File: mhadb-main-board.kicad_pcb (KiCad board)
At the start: 4 copper layers, 50 x 50 mm, 109 parts, among them J1 Conn_01x04, J10 Conn_01x04_Pin, J2 Conn_01x04, J3 USB_C_Receptacle_USB2.0_14P, J4 Conn_01x02, J5 Conn_01x03, J6 Conn_01x03, J7 Conn_01x04, J8 Conn_01x04, J9 Conn_01x02_Pin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

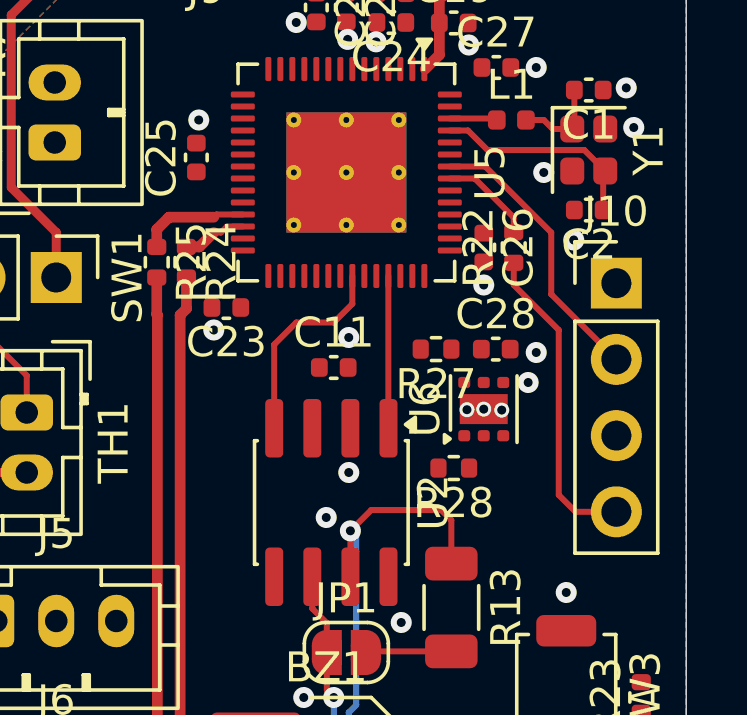
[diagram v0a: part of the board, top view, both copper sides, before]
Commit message: pcb: add I2C routing
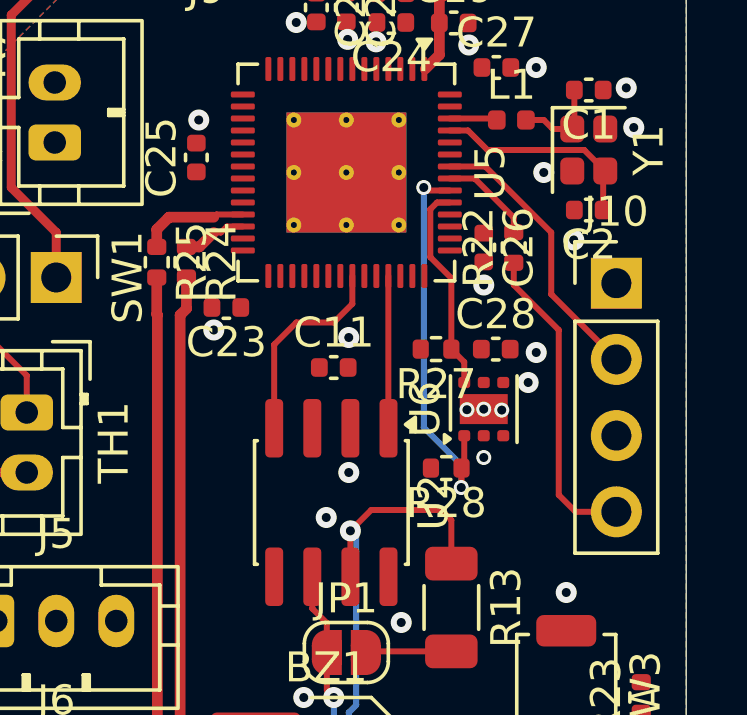
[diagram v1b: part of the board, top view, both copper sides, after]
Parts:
- moved R28 0.25 mm to (146.0, 73.4)
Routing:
- net /SCL: track 0.00 -> 13.2 mm, vias 0 -> 2
- net /SDA: track 0.00 -> 6.99 mm
- net GND: vias 59 -> 60
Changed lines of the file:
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@@
 	(footprint "Resistor_SMD:R_0402_1005Metric"
 		(layer "F.Cu")
-		(at 146.25 73.3525 180)
+		(at 146 73.3525 180)
 		(descr "Resistor SMD 0402 (1005 Metric), square (rectangular) end terminal, IPC-7351 nominal, (Body size source: IPC-SM-782 page 72, https://www.pcb-3d.com/wordpress/wp-content/uploads/ipc-sm-782a_amendment_1_and_2.pdf), generated with kicad-footprint-generator")
 		(tags "resistor")
@@
 	)
 	(via
+		(at 147.25 73)
+		(size 0.5)
+		(drill 0.3)
+		(layers "F.Cu" "B.Cu")
+		(free yes)
+		(net 5)
+	)
+	(via
 		(at 147.25 67.25)
 		(size 0.7)
@@
 		(net 64)
 	)
+	(segment
+		(start 146.6 70.5)
+		(end 146.6 69.8175)
+		(width 0.2)
+		(layer "F.Cu")
+		(net 75)
+	)
+	(segment
+		(start 146.6 69.8175)
+		(end 146.17 69.3875)
+		(width 0.2)
+		(layer "F.Cu")
+		(net 75)
+	)
+	(segment
+		(start 146.17 67.022936)
+		(end 145.469 66.321936)
+		(width 0.2)
+		(layer "F.Cu")
+		(net 75)
+	)
+	(segment
+		(start 145.469 64.723936)
+		(end 145.692936 64.5)
+		(width 0.2)
+		(layer "F.Cu")
+		(net 75)
+	)
+	(segment
+		(start 145.692936 64.5)
+		(end 146.12 64.5)
+		(width 0.2)
+		(layer "F.Cu")
+		(net 75)
+	)
+	(segment
+		(start 145.469 66.321936)
+		(end 145.469 64.723936)
+		(width 0.2)
+		(layer "F.Cu")
+		(net 75)
+	)
+	(segment
+		(start 146.17 69.3875)
+		(end 146.17 67.022936)
+		(width 0.2)
+		(layer "F.Cu")
+		(net 75)
+	)
+	(segment
+		(start 146.51 73.99)
+		(end 146.5 74)
+		(width 0.2)
+		(layer "F.Cu")
+		(net 86)
+	)
+	(segment
+		(start 146.6 72.275)
+		(end 146.6 73.2625)
+		(width 0.2)
+		(layer "F.Cu")
+		(net 86)
+	)
+	(segment
+		(start 145.35 64.1)
+		(end 146.12 64.1)
+		(width 0.2)
+		(layer "F.Cu")
+		(net 86)
+	)
+	(segment
+		(start 146.51 73.3525)
+		(end 146.51 73.99)
+		(width 0.2)
+		(layer "F.Cu")
+		(net 86)
+	)
+	(segment
+		(start 145.25 64)
+		(end 145.35 64.1)
+		(width 0.2)
+		(layer "F.Cu")
+		(net 86)
+	)
+	(segment
+		(start 146.6 73.2625)
+		(end 146.51 73.3525)
+		(width 0.2)
+		(layer "F.Cu")
+		(net 86)
+	)
+	(via
+		(at 146.5 74)
+		(size 0.5)
+		(drill 0.3)
+		(layers "F.Cu" "B.Cu")
+		(net 86)
+	)
+	(via
+		(at 145.25 64)
+		(size 0.5)
+		(drill 0.3)
+		(layers "F.Cu" "B.Cu")
+		(net 86)
+	)
+	(segment
+		(start 145.25 72)
+		(end 145.25 64)
+		(width 0.2)
+		(layer "B.Cu")
+		(net 86)
+	)
+	(segment
+		(start 146.5 74)
+		(end 146.5 73.25)
+		(width 0.2)
+		(layer "B.Cu")
+		(net 86)
+	)
+	(segment
+		(start 146.5 73.25)
+		(end 145.25 72)
+		(width 0.2)
+		(layer "B.Cu")
+		(net 86)
+	)
 	(zone

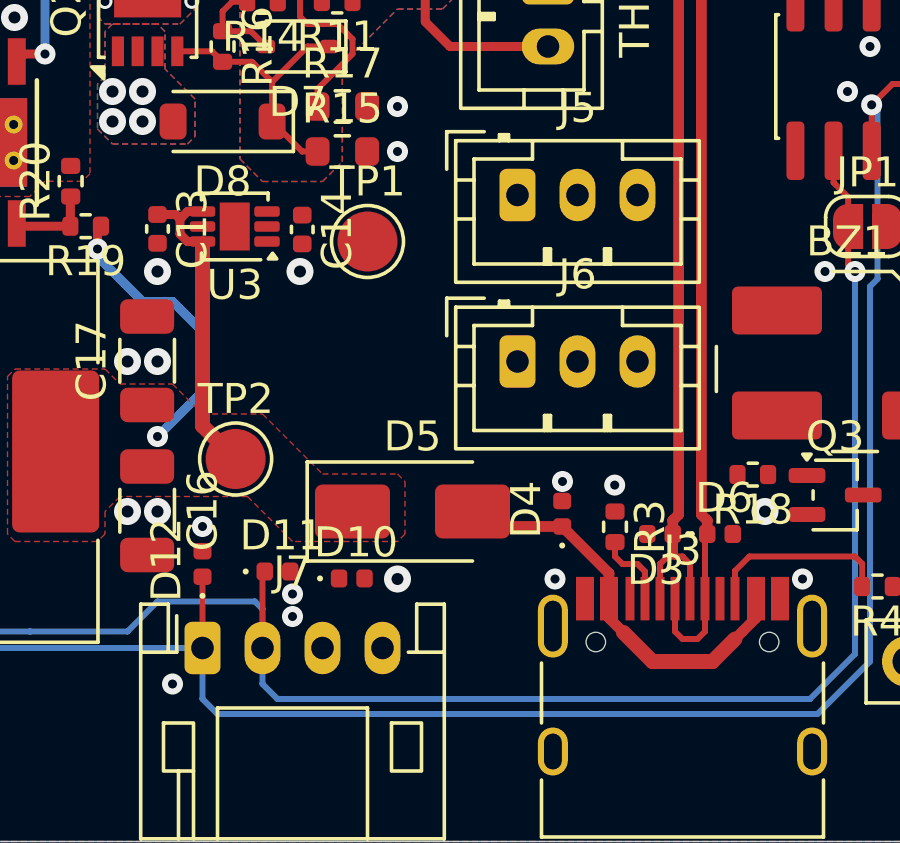
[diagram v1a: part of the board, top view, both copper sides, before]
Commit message: pcb: add 5v pwr routing
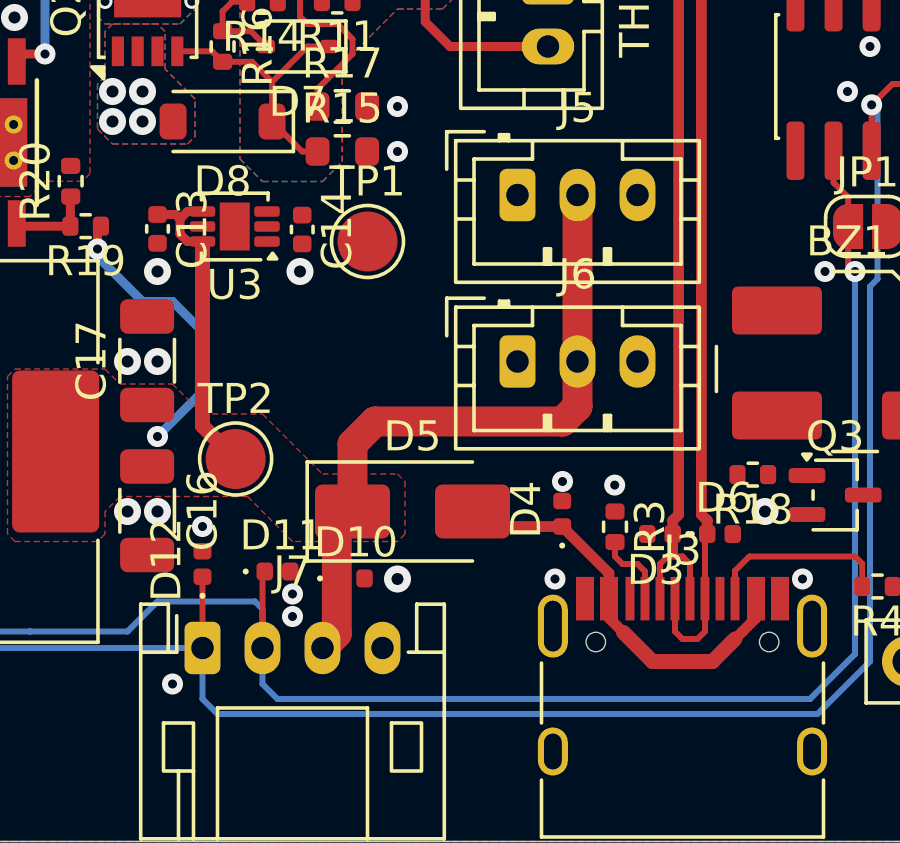
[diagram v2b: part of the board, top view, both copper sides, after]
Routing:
- net +5V: track 20.4 -> 42.6 mm
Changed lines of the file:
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@@
+	)
+	(segment
+		(start 125.5 89)
+		(end 124.975952 89.524048)
+		(width 1)
+		(layer "F.Cu")
+		(net 16)
 	)
 	(segment
@@
 		(end 120.5 86.145)
 		(width 0.5)
+		(layer "F.Cu")
+		(net 16)
+	)
+	(segment
+		(start 132.5 86)
+		(end 133 85.5)
+		(width 1)
 		(layer "F.Cu")
 		(net 16)
@@
 	)
 	(segment
+		(start 125.5 89)
+		(end 125.5 86.75)
+		(width 1)
+		(layer "F.Cu")
+		(net 16)
+	)
+	(segment
 		(start 117 79.605)
 		(end 117.115 79.49)
 		(width 0.3)
+		(layer "F.Cu")
+		(net 16)
+	)
+	(segment
+		(start 124.975952 89.524048)
+		(end 124.975952 93.074048)
+		(width 1)
+		(layer "F.Cu")
+		(net 16)
+	)
+	(segment
+		(start 126.25 86)
+		(end 132.5 86)
+		(width 1)
 		(layer "F.Cu")
 		(net 16)
@@
 		(end 117 79.605)
 		(width 0.3)
+		(layer "F.Cu")
+		(net 16)
+	)
+	(segment
+		(start 125.5 86.75)
+		(end 126.25 86)
+		(width 1)
 		(layer "F.Cu")
 		(net 16)
@@
 		(layer "F.Cu")
 		(net 16)
+	)
+	(segment
+		(start 124.975952 93.074048)
+		(end 124.5 93.55)
+		(width 1)
+		(layer "F.Cu")
+		(net 16)
+	)
+	(segment
+		(start 133 84)
+		(end 133 78.45)
+		(width 1)
+		(layer "F.Cu")
+		(net 16)
+	)
+	(segment
+		(start 133 85.5)
+		(end 133 84)
+		(width 1)
+		(layer "F.Cu")
+		(net 16)

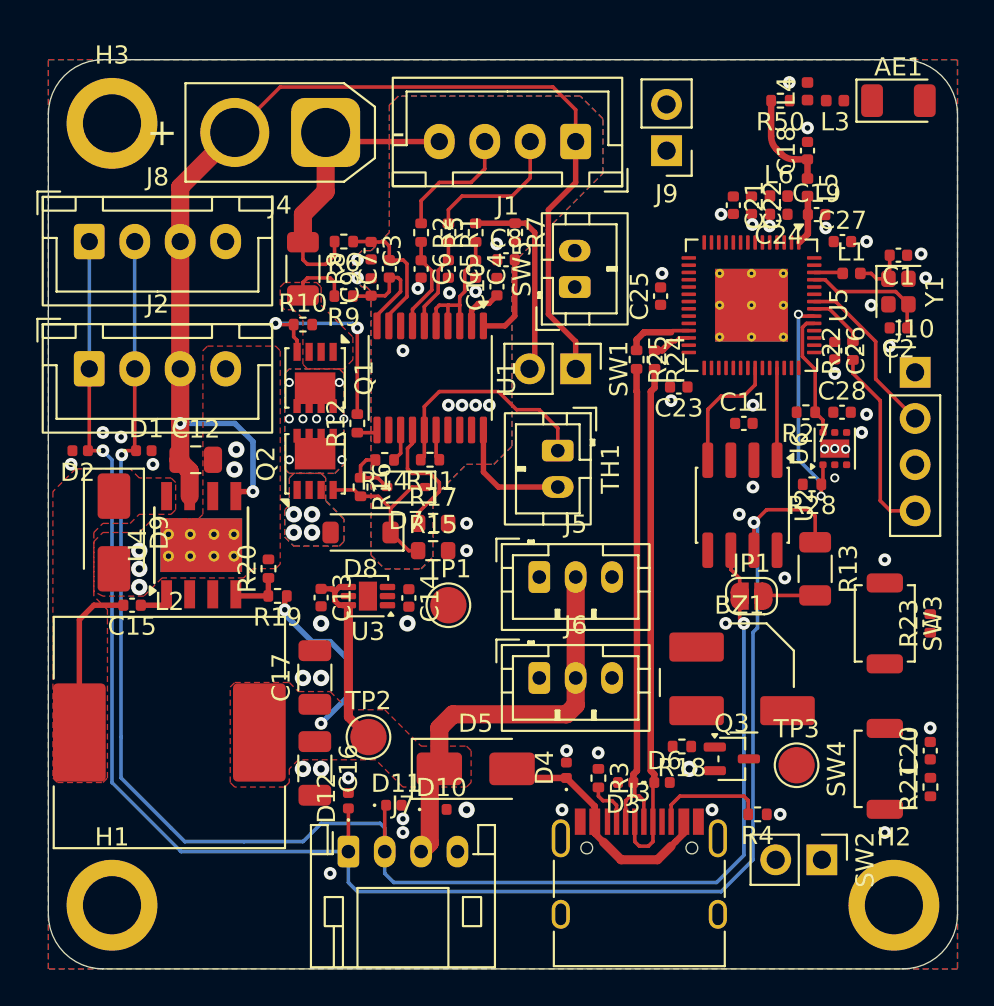
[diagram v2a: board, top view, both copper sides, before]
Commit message: pcb: add 3V3 pwr routing
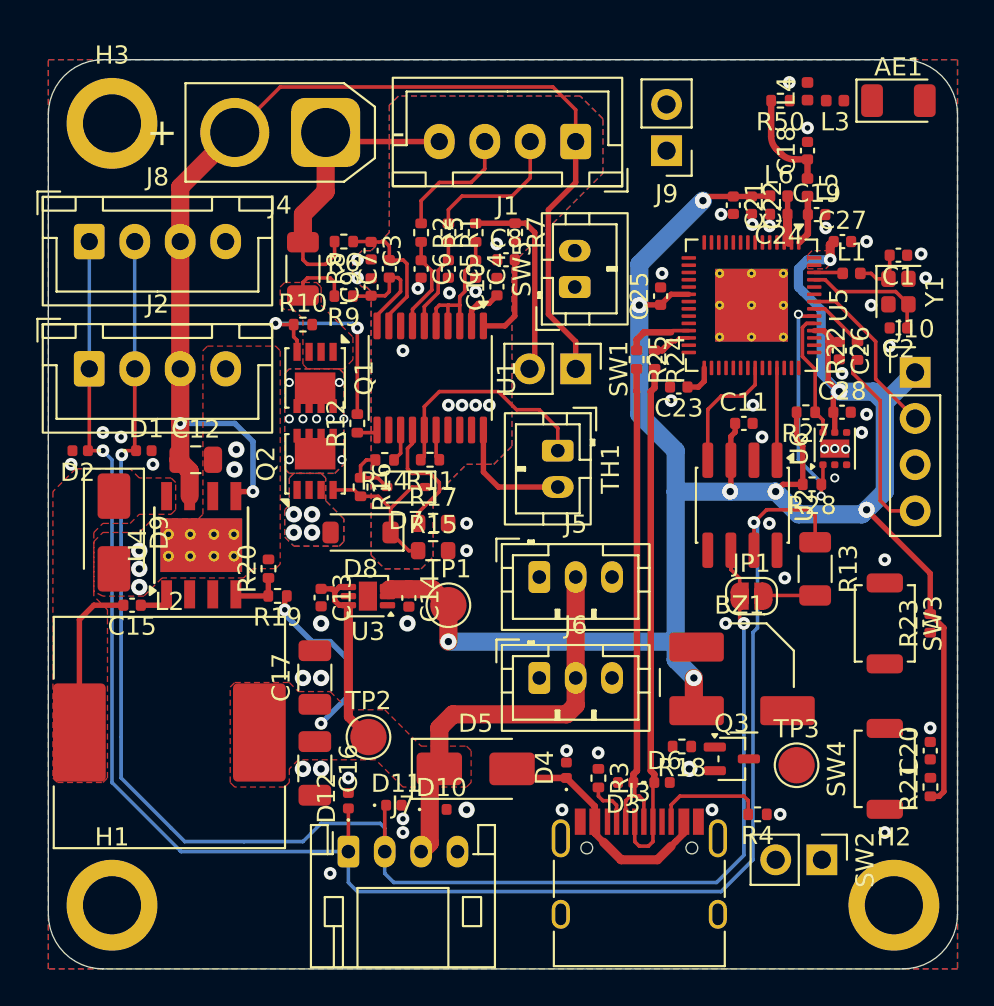
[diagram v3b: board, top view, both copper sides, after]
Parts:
- moved C26 0.25 mm to (147.5, 66.0)
- moved R22 0.25 mm to (148.5, 66.0)
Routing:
- net +3V3: track 0.00 -> 125.6 mm, vias 0 -> 9
- net VDD3P3: track 0.00 -> 2.58 mm
- net /VDD_SPI: track 0.00 -> 1.78 mm
- added copper zone on F.Cu, net +3V3

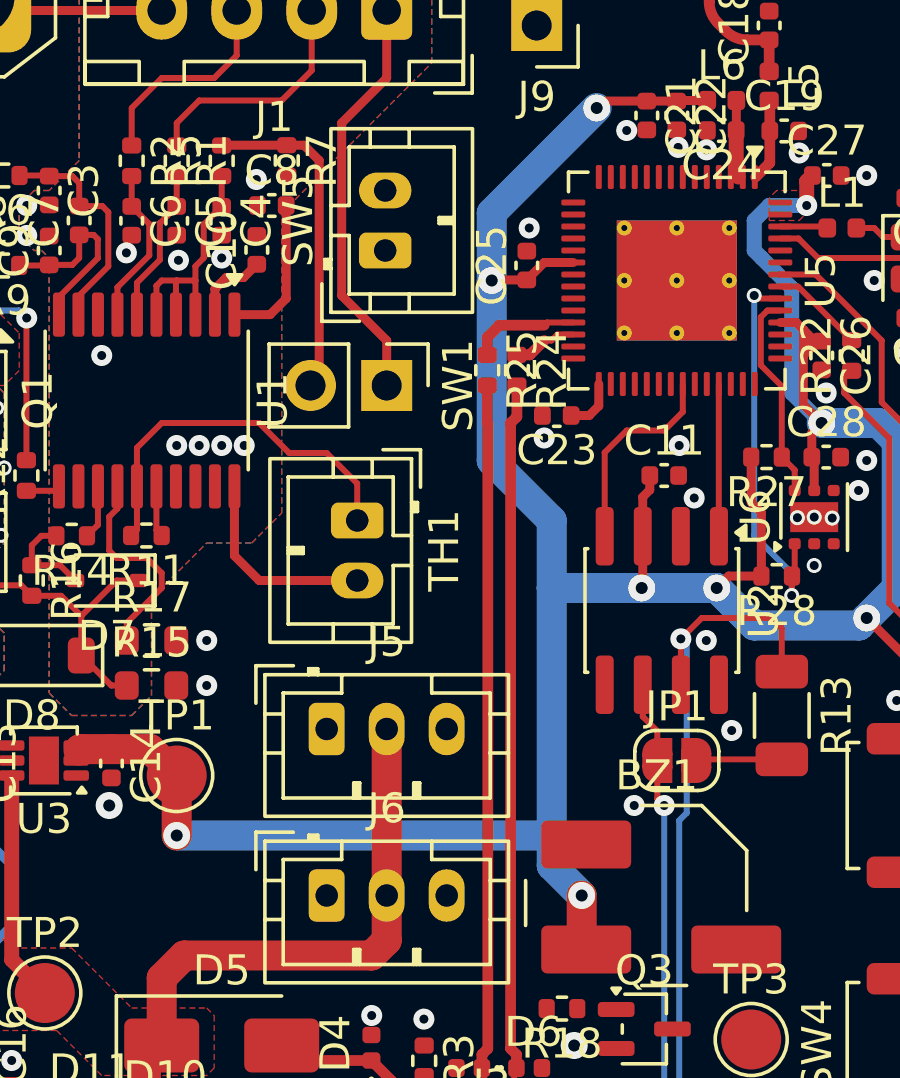
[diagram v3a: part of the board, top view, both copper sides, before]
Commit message: pcb: add RGB connectors routing
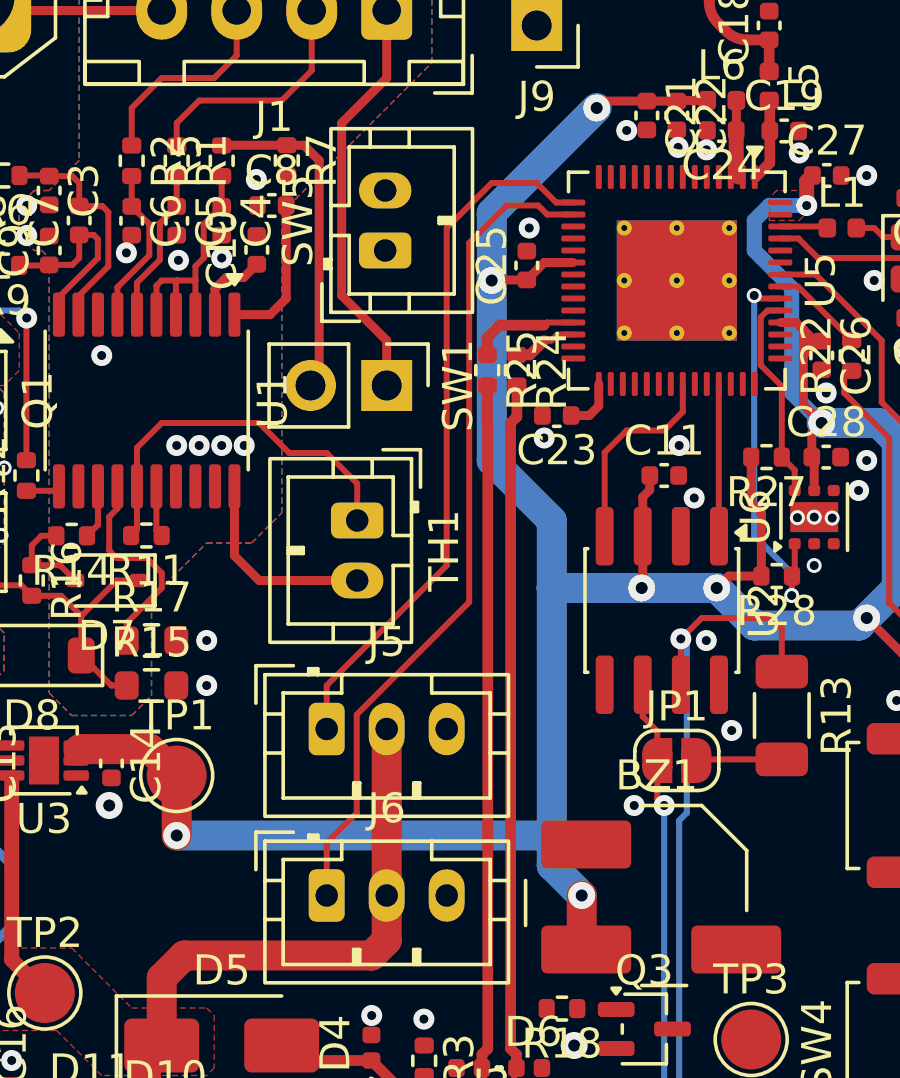
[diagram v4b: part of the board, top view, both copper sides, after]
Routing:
- net /RGB2: track 0.00 -> 27.8 mm
- net /RGB1: track 0.00 -> 23.5 mm
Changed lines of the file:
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@@
+	)
+	(segment
+		(start 138.65 60.9)
+		(end 139.22 60.9)
+		(width 0.2)
+		(layer "F.Cu")
+		(net 35)
+	)
+	(segment
+		(start 131 77)
+		(end 135 73)
+		(width 0.2)
+		(layer "F.Cu")
+		(net 35)
+	)
+	(segment
+		(start 138 60.25)
+		(end 138.65 60.9)
+		(width 0.2)
+		(layer "F.Cu")
+		(net 35)
+	)
+	(segment
+		(start 131 78.45)
+		(end 131 77)
+		(width 0.2)
+		(layer "F.Cu")
+		(net 35)
+	)
+	(segment
+		(start 136.5 60.25)
+		(end 138 60.25)
+		(width 0.2)
+		(layer "F.Cu")
+		(net 35)
+	)
+	(segment
+		(start 135 73)
+		(end 135 61.75)
+		(width 0.2)
+		(layer "F.Cu")
+		(net 35)
+	)
+	(segment
+		(start 135 61.75)
+		(end 136.5 60.25)
+		(width 0.2)
+		(layer "F.Cu")
+		(net 35)
+	)
+	(segment
+		(start 132 81.25)
+		(end 131 82.25)
+		(width 0.2)
+		(layer "F.Cu")
+		(net 36)
+	)
+	(segment
+		(start 135.75 62.25)
+		(end 135.75 74.221504)
+		(width 0.2)
+		(layer "F.Cu")
+		(net 36)
+	)
+	(segment
+		(start 137 61)
+		(end 135.75 62.25)
+		(width 0.2)
+		(layer "F.Cu")
+		(net 36)
+	)
+	(segment
+		(start 138.350057 61.3)
+		(end 138.050057 61)
+		(width 0.2)
+		(layer "F.Cu")
+		(net 36)
+	)
+	(segment
+		(start 132 77.971504)
+		(end 132 81.25)
+		(width 0.2)
+		(layer "F.Cu")
+		(net 36)
+	)
+	(segment
+		(start 138.050057 61)
+		(end 137 61)
+		(width 0.2)
+		(layer "F.Cu")
+		(net 36)
+	)
+	(segment
+		(start 131 82.25)
+		(end 131 84)
+		(width 0.2)
+		(layer "F.Cu")
+		(net 36)
+	)
+	(segment
+		(start 139.22 61.3)
+		(end 138.350057 61.3)
+		(width 0.2)
+		(layer "F.Cu")
+		(net 36)
+	)
+	(segment
+		(start 135.75 74.221504)
+		(end 132 77.971504)
+		(width 0.2)
+		(layer "F.Cu")
+		(net 36)
 	)
 	(segment
